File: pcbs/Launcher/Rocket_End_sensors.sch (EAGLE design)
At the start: 9 parts, among them U1 ARDUINO-MEGAPRO-5V, X1 22-23-2051, X3 22-23-2041, X5 22-23-2101, X6 22-23-2101, X7 22-23-2101, X8 22-23-2031

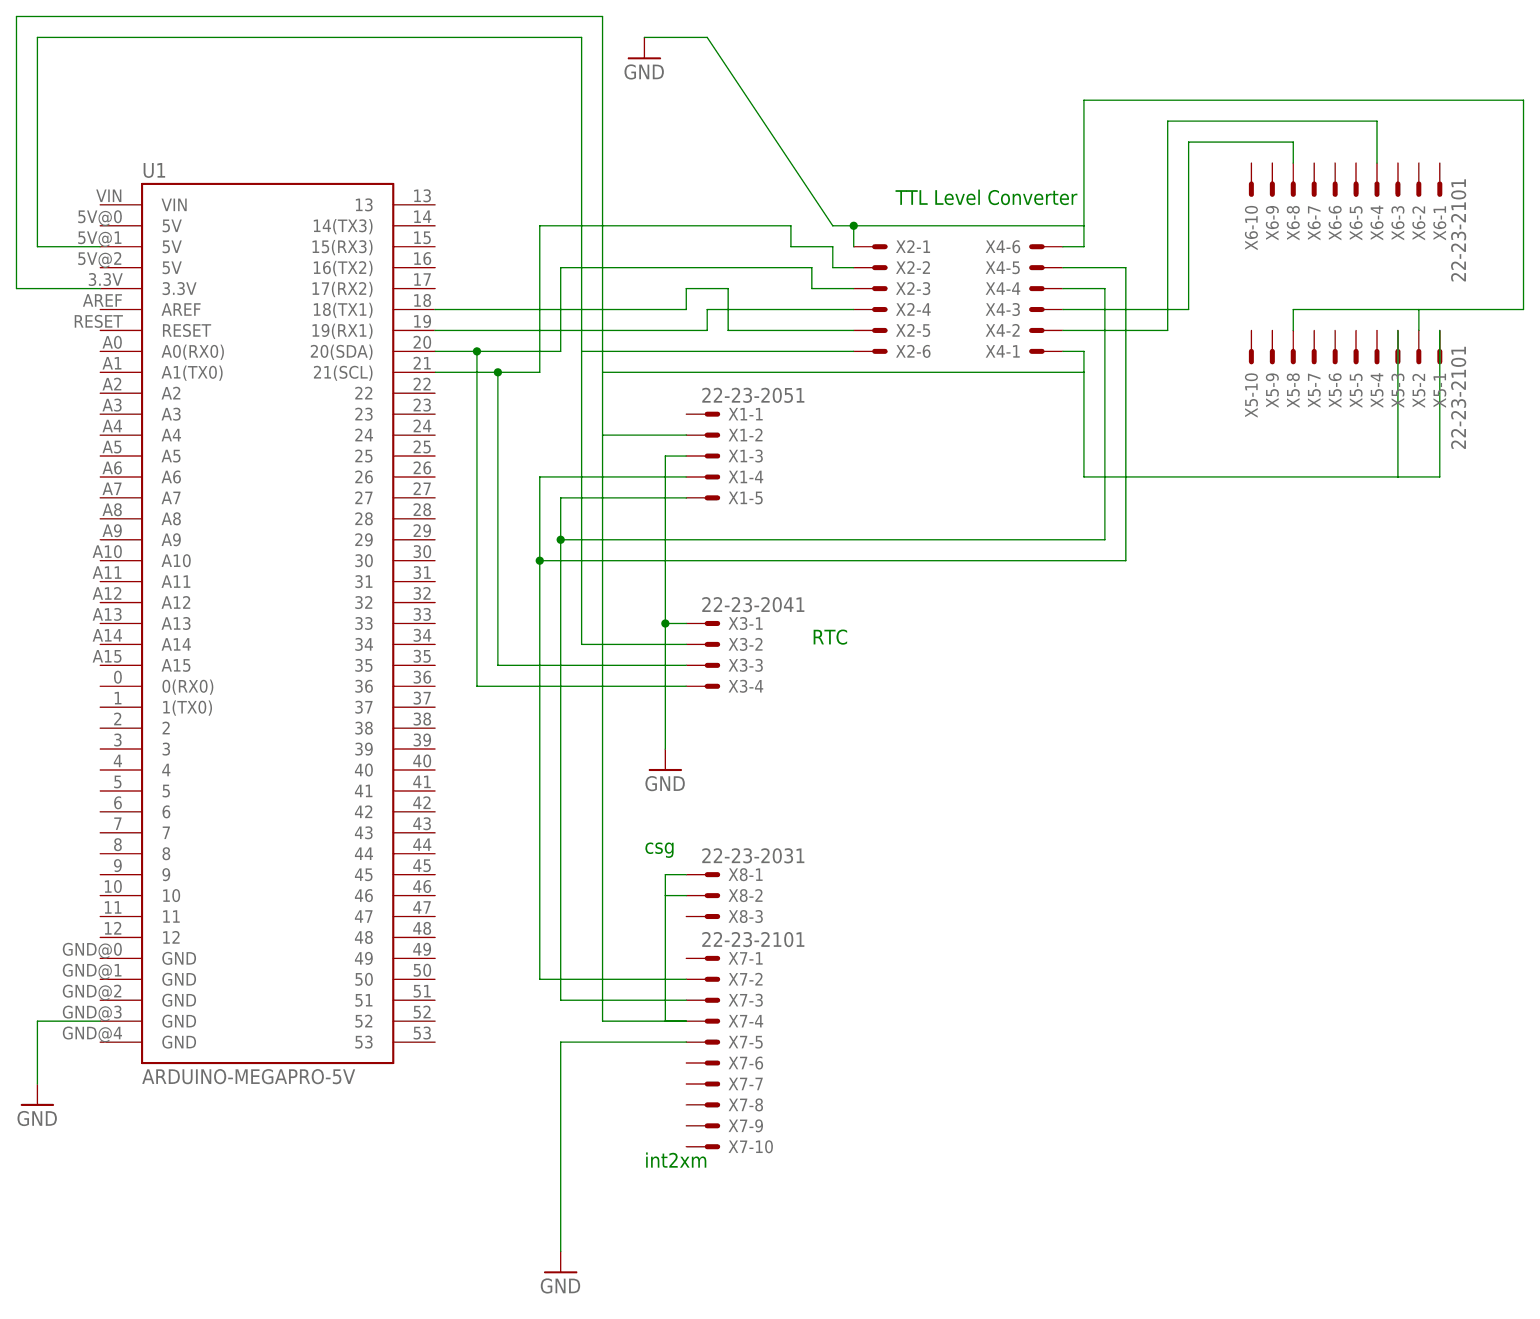
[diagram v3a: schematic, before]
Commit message: * More space between tracks * Ground wire added to GPS module * Added extra holes, so we can do some hacks alter on the IMU
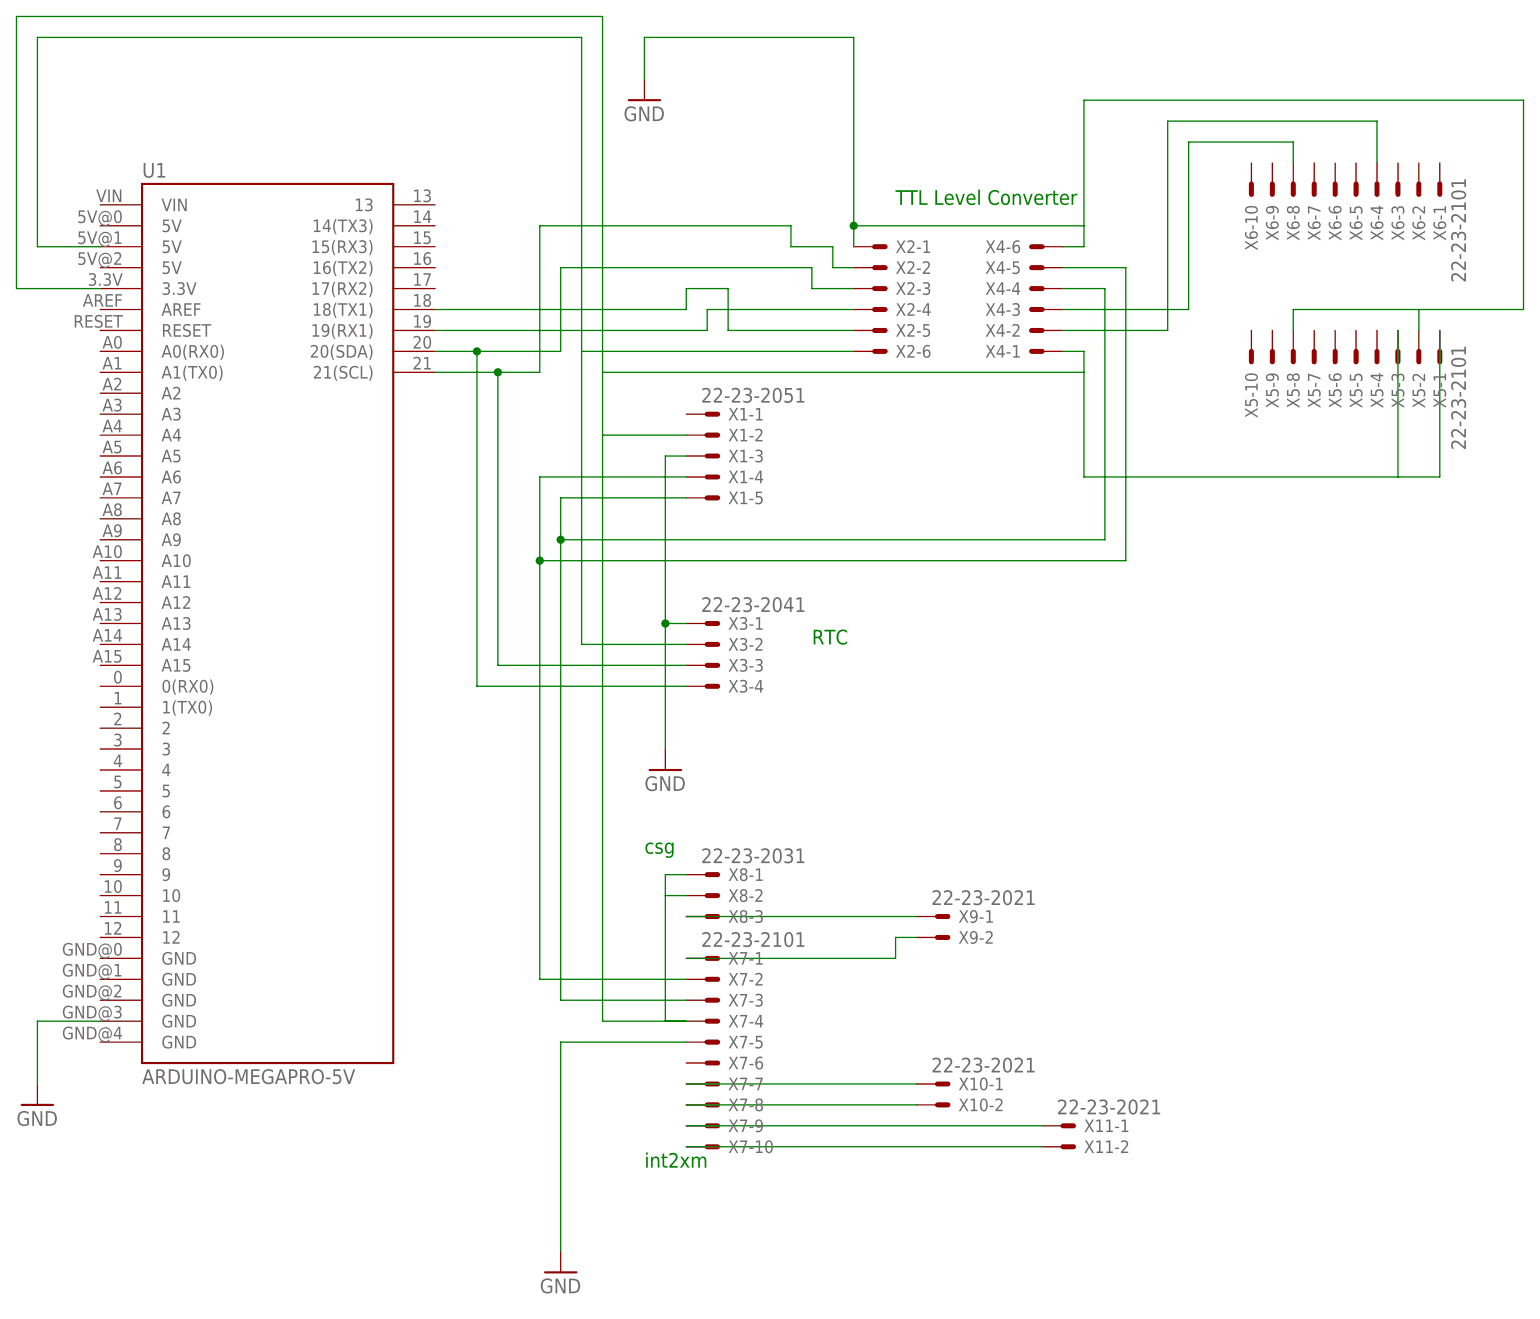
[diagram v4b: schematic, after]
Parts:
- added X10, X11, X9: 22-23-2021, con-molex:22-23-2021
- U1: device SparkFun-Boards:ARDUINO-MEGAPRO-5V -> JoeMega_Ether_Edited:ARDUINO-MEGAPRO-5V
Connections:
- new net N$10: X10-1.S, X7-7.S
- new net N$11: X10-2.S, X7-8.S
- new net N$12: X11-1.S, X7-9.S
- new net N$13: X11-2.S, X7-10.S
- new net N$9: X7-1.S, X9-2.S
- net GND: now also X2-1.S, X4-6.S, X5-2.S, X5-8.S
- net N$7: now also X8-3.S, X9-1.S; no longer X2-1.S, X4-6.S, X5-2.S, X5-8.S
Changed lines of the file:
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@@
 <?xml version="1.0" encoding="utf-8"?>
 <!DOCTYPE eagle SYSTEM "eagle.dtd">
-<eagle version="7.1.0">
+<eagle version="7.3.0">
 <drawing>
 <settings>
@@
 </classes>
 <parts>
-<part name="U1" library="SparkFun-Boards" deviceset="ARDUINO-MEGA" device="PRO-5V"/>
+<part name="U1" library="JoeMega_Ether_Edited" deviceset="ARDUINO-MEGA" device="PRO-5V"/>
 <part name="GND7" library="supply1" deviceset="GND" device=""/>
 <part name="X3" library="con-molex" deviceset="22-23-2041" device=""/>
@@
 <part name="GND3" library="supply1" deviceset="GND" device=""/>
 <part name="X5" library="con-molex" deviceset="22-23-2101" device=""/>
+<part name="X9" library="con-molex" deviceset="22-23-2021" device=""/>
+<part name="X10" library="con-molex" deviceset="22-23-2021" device=""/>
+<part name="X11" library="con-molex" deviceset="22-23-2021" device=""/>
 </parts>
 <sheets>
@@
 <instance part="X4" gate="-5" x="132.08" y="96.52" rot="R180"/>
 <instance part="X4" gate="-6" x="132.08" y="99.06" rot="R180"/>
-<instance part="GND2" gate="1" x="83.82" y="121.92"/>
+<instance part="GND2" gate="1" x="83.82" y="116.84"/>
 <instance part="X6" gate="-1" x="180.34" y="106.68" rot="R270"/>
 <instance part="X6" gate="-2" x="177.8" y="106.68" rot="R270"/>
@@
 <instance part="X5" gate="-9" x="160.02" y="86.36" rot="R270"/>
 <instance part="X5" gate="-10" x="157.48" y="86.36" rot="R270"/>
+<instance part="X9" gate="-1" x="119.38" y="17.78"/>
+<instance part="X9" gate="-2" x="119.38" y="15.24"/>
+<instance part="X10" gate="-1" x="119.38" y="-2.54"/>
+<instance part="X10" gate="-2" x="119.38" y="-5.08"/>
+<instance part="X11" gate="-1" x="134.62" y="-7.62"/>
+<instance part="X11" gate="-2" x="134.62" y="-10.16"/>
 </instances>
 <busses>
@@
 </segment>
 <segment>
-<wire x1="106.68" y1="101.6" x2="91.44" y2="124.46" width="0.1524" layer="91"/>
-<wire x1="91.44" y1="124.46" x2="83.82" y2="124.46" width="0.1524" layer="91"/>
-<pinref part="GND2" gate="1" pin="GND"/>
-</segment>
-<segment>
 <pinref part="X7" gate="-5" pin="S"/>
 <wire x1="88.9" y1="2.54" x2="73.66" y2="2.54" width="0.1524" layer="91"/>
 <wire x1="73.66" y1="2.54" x2="73.66" y2="-22.86" width="0.1524" layer="91"/>
 <pinref part="GND3" gate="1" pin="GND"/>
+</segment>
+<segment>
+<pinref part="X4" gate="-6" pin="S"/>
+<wire x1="134.62" y1="99.06" x2="137.16" y2="99.06" width="0.1524" layer="91"/>
+<wire x1="137.16" y1="99.06" x2="137.16" y2="101.6" width="0.1524" layer="91"/>
+<wire x1="137.16" y1="101.6" x2="109.22" y2="101.6" width="0.1524" layer="91"/>
+<pinref part="X2" gate="-1" pin="S"/>
+<wire x1="190.5" y1="91.44" x2="177.8" y2="91.44" width="0.1524" layer="91"/>
+<wire x1="177.8" y1="91.44" x2="162.56" y2="91.44" width="0.1524" layer="91"/>
+<wire x1="190.5" y1="91.44" x2="190.5" y2="116.84" width="0.1524" layer="91"/>
+<wire x1="190.5" y1="116.84" x2="137.16" y2="116.84" width="0.1524" layer="91"/>
+<wire x1="137.16" y1="116.84" x2="137.16" y2="101.6" width="0.1524" layer="91"/>
+<wire x1="109.22" y1="99.06" x2="109.22" y2="101.6" width="0.1524" layer="91"/>
+<wire x1="109.22" y1="101.6" x2="109.22" y2="124.46" width="0.1524" layer="91"/>
+<junction x="109.22" y="101.6"/>
+<pinref part="X5" gate="-2" pin="S"/>
+<wire x1="177.8" y1="88.9" x2="177.8" y2="91.44" width="0.1524" layer="91"/>
+<pinref part="X5" gate="-8" pin="S"/>
+<wire x1="162.56" y1="88.9" x2="162.56" y2="91.44" width="0.1524" layer="91"/>
+<wire x1="109.22" y1="124.46" x2="83.82" y2="124.46" width="0.1524" layer="91"/>
+<pinref part="GND2" gate="1" pin="GND"/>
+<wire x1="83.82" y1="124.46" x2="83.82" y2="119.38" width="0.1524" layer="91"/>
 </segment>
 </net>
@@
 <net name="N$7" class="0">
 <segment>
-<pinref part="X4" gate="-6" pin="S"/>
-<wire x1="134.62" y1="99.06" x2="137.16" y2="99.06" width="0.1524" layer="91"/>
-<wire x1="137.16" y1="99.06" x2="137.16" y2="101.6" width="0.1524" layer="91"/>
-<wire x1="137.16" y1="101.6" x2="109.22" y2="101.6" width="0.1524" layer="91"/>
-<pinref part="X2" gate="-1" pin="S"/>
-<wire x1="190.5" y1="91.44" x2="177.8" y2="91.44" width="0.1524" layer="91"/>
-<wire x1="177.8" y1="91.44" x2="162.56" y2="91.44" width="0.1524" layer="91"/>
-<wire x1="190.5" y1="91.44" x2="190.5" y2="116.84" width="0.1524" layer="91"/>
-<wire x1="190.5" y1="116.84" x2="137.16" y2="116.84" width="0.1524" layer="91"/>
-<wire x1="137.16" y1="116.84" x2="137.16" y2="101.6" width="0.1524" layer="91"/>
-<wire x1="109.22" y1="99.06" x2="109.22" y2="101.6" width="0.1524" layer="91"/>
-<wire x1="109.22" y1="101.6" x2="106.68" y2="101.6" width="0.1524" layer="91"/>
-<junction x="109.22" y="101.6"/>
-<pinref part="X5" gate="-2" pin="S"/>
-<wire x1="177.8" y1="88.9" x2="177.8" y2="91.44" width="0.1524" layer="91"/>
-<pinref part="X5" gate="-8" pin="S"/>
-<wire x1="162.56" y1="88.9" x2="162.56" y2="91.44" width="0.1524" layer="91"/>
-</segment>
-</net>
+<pinref part="X8" gate="-3" pin="S"/>
+<pinref part="X9" gate="-1" pin="S"/>
+<wire x1="88.9" y1="17.78" x2="116.84" y2="17.78" width="0.1524" layer="91"/>
+</segment>
+</net>
+<net name="N$9" class="0">
+<segment>
+<pinref part="X7" gate="-1" pin="S"/>
+<wire x1="88.9" y1="12.7" x2="114.3" y2="12.7" width="0.1524" layer="91"/>
+<wire x1="114.3" y1="12.7" x2="114.3" y2="15.24" width="0.1524" layer="91"/>
+<pinref part="X9" gate="-2" pin="S"/>
+<wire x1="114.3" y1="15.24" x2="116.84" y2="15.24" width="0.1524" layer="91"/>
+</segment>
+</net>
+<net name="N$10" class="0">
+<segment>
+<pinref part="X7" gate="-7" pin="S"/>
+<pinref part="X10" gate="-1" pin="S"/>
+<wire x1="88.9" y1="-2.54" x2="116.84" y2="-2.54" width="0.1524" layer="91"/>
+</segment>
+</net>
+<net name="N$11" class="0">
+<segment>
+<pinref part="X7" gate="-8" pin="S"/>
+<pinref part="X10" gate="-2" pin="S"/>
+<wire x1="88.9" y1="-5.08" x2="116.84" y2="-5.08" width="0.1524" layer="91"/>
+</segment>
+</net>
+<net name="N$12" class="0">
+<segment>
+<pinref part="X7" gate="-9" pin="S"/>
+<pinref part="X11" gate="-1" pin="S"/>
+<wire x1="88.9" y1="-7.62" x2="132.08" y2="-7.62" width="0.1524" layer="91"/>
+</segment>
+</net>
+<net name="N$13" class="0">
+<segment>
+<pinref part="X7" gate="-10" pin="S"/>
+<pinref part="X11" gate="-2" pin="S"/>
+<wire x1="88.9" y1="-10.16" x2="132.08" y2="-10.16" width="0.1524" layer="91"/>
+</segment>
+</net>
